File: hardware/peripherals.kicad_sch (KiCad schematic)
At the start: 25 parts, among them J6 Conn_01x02, J7 Conn_01x03, J8 USB_C_Receptacle_USB2.0_14P, SW1 SW_Push, U3 74AHCT1G125, U4 USBLC6-2SC6, U5 DS3231MZ

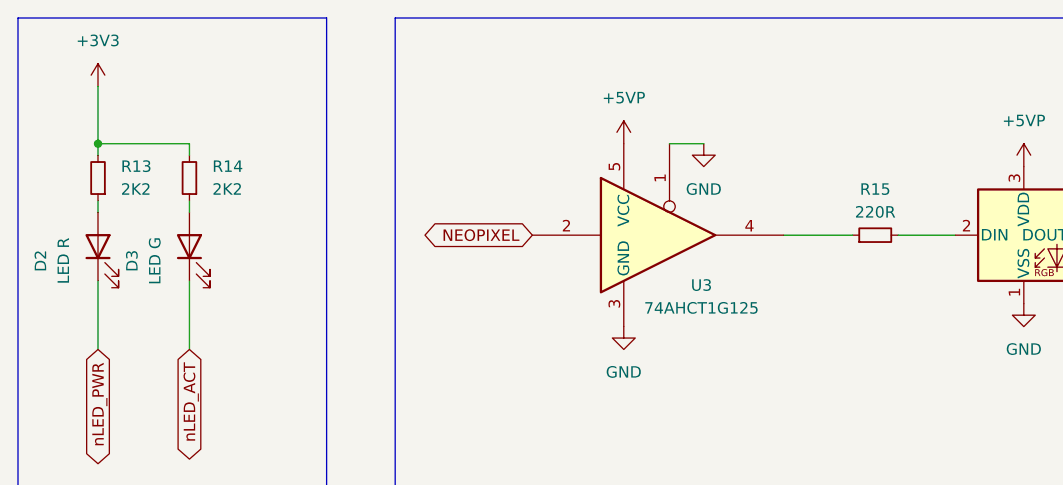
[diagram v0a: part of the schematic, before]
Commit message: Consolidate LED resistors to 330R, eliminate 220R value
R13, R14 (status LEDs): 2K2 → 330R
R15 (NeoPixel data): 220R → 330R
9 unique resistor values (was 10)
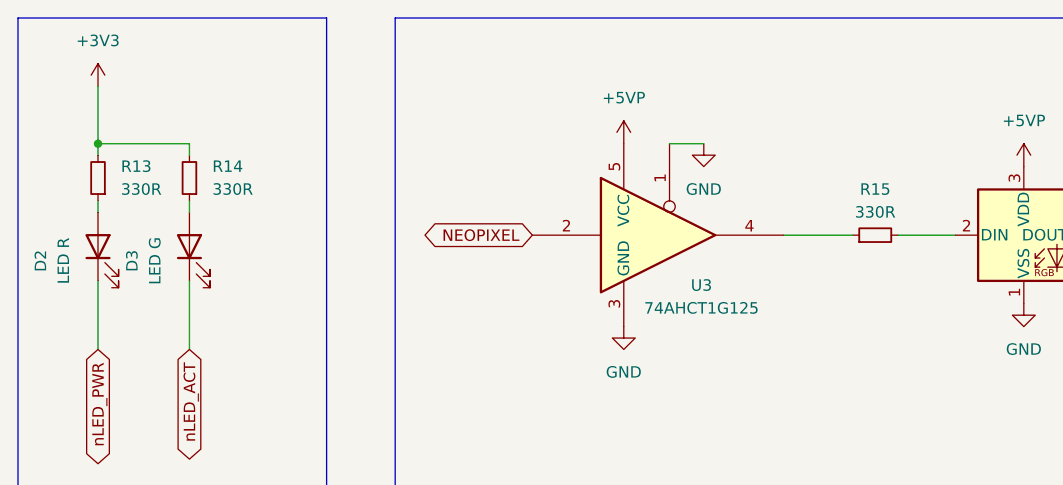
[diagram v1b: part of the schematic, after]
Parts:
- R13, R14: value 2K2 -> 330R
- R15: value 220R -> 330R
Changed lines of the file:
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@@
 			)
 		)
-		(property "Value" "2K2"
+		(property "Value" "330R"
 			(at 36.83 34.2899 0)
 			(show_name no)
@@
 			)
 		)
-		(property "Value" "2K2"
+		(property "Value" "330R"
 			(at 26.67 34.2899 0)
 			(show_name no)
@@
 			)
 		)
-		(property "Value" "220R"
+		(property "Value" "330R"
 			(at 110.49 36.83 90)
 			(show_name no)

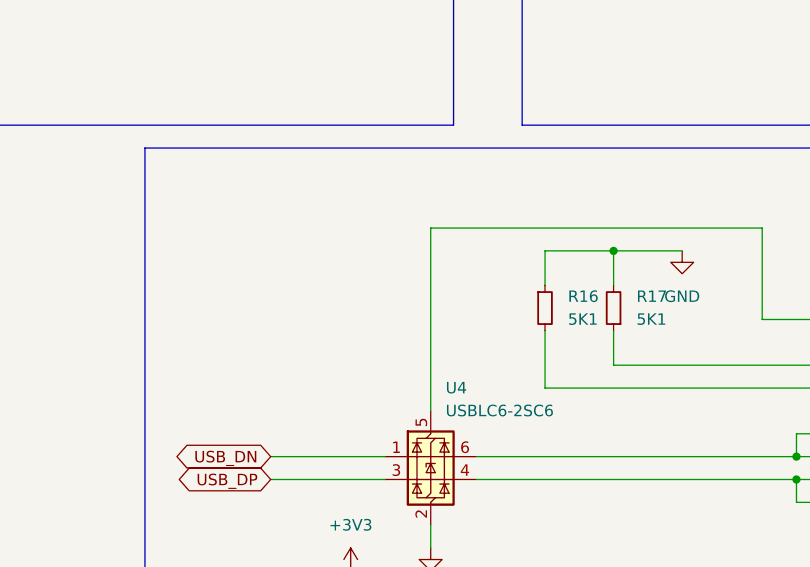
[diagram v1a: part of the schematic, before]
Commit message: Add 100nF decoupling cap on USB VBUS for USBLC6-2SC6
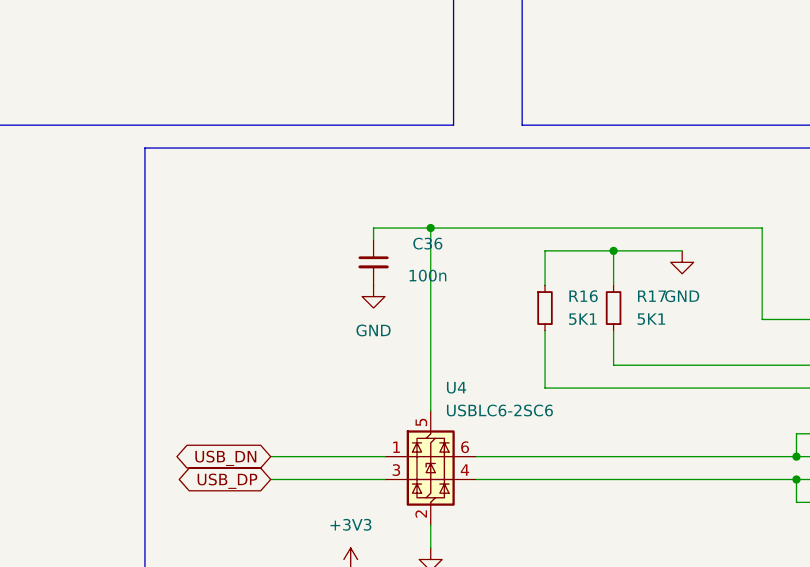
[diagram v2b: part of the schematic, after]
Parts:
- added C36: 100n, Capacitor_SMD:C_0805_2012Metric, symbol Device:C_Small
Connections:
- net GND: now also C36.2
- net at J8.A4 (VBUS), J8.A9 (VBUS), J8.B4 (VBUS)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: now also C36.1
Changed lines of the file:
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@@
 	)
 	(junction
+		(at 161.29 81.28)
+		(diameter 0)
+		(color 0 0 0 0)
+	)
+	(junction
 		(at 24.13 29.21)
 		(diameter 0)
@@
 	(wire
 		(pts
+			(xy 154.94 82.55) (xy 154.94 81.28)
+		)
+		(stroke
+			(width 0)
+			(type default)
+		)
+	)
+	(wire
+		(pts
 			(xy 173.99 83.82) (xy 181.61 83.82)
 		)
@@
 	(wire
 		(pts
+			(xy 154.94 81.28) (xy 161.29 81.28)
+		)
+		(stroke
+			(width 0)
+			(type default)
+		)
+	)
+	(wire
+		(pts
 			(xy 166.37 109.22) (xy 201.93 109.22)
 		)
@@
 	(symbol
 		(lib_id "power:GND")
+		(at 154.94 87.63 0)
+		(unit 1)
+		(body_style 1)
+		(exclude_from_sim no)
+		(in_bom yes)
+		(on_board yes)
+		(in_pos_files yes)
+		(dnp no)
+		(fields_autoplaced yes)
+		(property "Reference" "#PWR073"
+			(at 154.94 93.98 0)
+			(hide yes)
+			(show_name no)
+			(do_not_autoplace no)
+			(effects
+				(font
+					(size 1.27 1.27)
+				)
+			)
+		)
+		(property "Value" "GND"
+			(at 154.94 92.71 0)
+			(show_name no)
+			(do_not_autoplace no)
+			(effects
+				(font
+					(size 1.27 1.27)
+				)
+			)
+		)
+		(property "Footprint" ""
+			(at 154.94 87.63 0)
+			(hide yes)
+			(show_name no)
+			(do_not_autoplace no)
+			(effects
+				(font
+					(size 1.27 1.27)
+				)
+			)
+		)
+		(property "Datasheet" ""
+			(at 154.94 87.63 0)
+			(hide yes)
+			(show_name no)
+			(do_not_autoplace no)
+			(effects
+				(font
+					(size 1.27 1.27)
+				)
+			)
+		)
+		(property "Description" "Power symbol creates a global label with name \"GND\" , ground"
+			(at 154.94 87.63 0)
+			(hide yes)
+			(show_name no)
+			(do_not_autoplace no)
+			(effects
+				(font
+					(size 1.27 1.27)
+				)
+			)
+		)
+		(pin "1"
+		)
+		(instances
+			(project "granit"
+				(path "/d2c135e3-a983-4cd4-8cff-b50ca3c7671a/d4e5f6a7-b8c9-4d0e-1f2a-3b4c5d6e7f80"
+					(reference "#PWR073")
+					(unit 1)
+				)
+			)
+		)
+	)
+	(symbol
+		(lib_id "power:GND")
 		(at 91.44 29.21 0)
 		(unit 1)
@@
 					(unit 1)
 				)
+			)
+		)
+	)
+	(symbol
+		(lib_id "Device:C_Small")
+		(at 154.94 85.09 0)
+		(unit 1)
+		(body_style 1)
+		(exclude_from_sim no)
+		(in_bom yes)
+		(on_board yes)
+		(in_pos_files yes)
+		(dnp no)
+		(property "Reference" "C36"
+			(at 159.258 83.058 0)
+			(show_name no)
+			(do_not_autoplace no)
+			(effects
+				(font
+					(size 1.27 1.27)
+				)
+				(justify left)
+			)
+		)
+		(property "Value" "100n"
+			(at 158.75 86.614 0)
+			(show_name no)
+			(do_not_autoplace no)
+			(effects
+				(font
+					(size 1.27 1.27)
+				)
+				(justify left)
+			)
+		)
+		(property "Footprint" "Capacitor_SMD:C_0805_2012Metric"
+			(at 155.9052 88.9 0)
+			(hide yes)
+			(show_name no)
+			(do_not_autoplace no)
+			(effects
+				(font
+					(size 1.27 1.27)
+				)
+			)
+		)
+		(property "Datasheet" "https://www.samsungsem.com/resources/file/global/support/product_catalog/MLCC.pdf"
+			(at 154.94 85.09 0)
+			(hide yes)
+			(show_name no)
+			(do_not_autoplace no)
+			(effects
+				(font
+					(size 1.27 1.27)
+				)
+			)
+		)
+		(property "Description" "RGB addressable LED (NeoPixel compatible)"
+			(at 154.94 85.09 0)
+			(hide yes)
+			(show_name no)
+			(do_not_autoplace no)
+			(effects
+				(font
+					(size 1.27 1.27)
+				)
+			)
+		)
+		(property "Supplier" "https://www.digikey.ch/de/products/detail/samsung-electro-mechanics/CL21B104KBCNNNC/3886661"
+			(at 154.94 85.09 0)
+			(hide yes)
+			(show_name no)
+			(do_not_autoplace no)
+			(effects
+				(font
+					(size 1.27 1.27)
+				)
+			)
+		)
+		(property "Notes" "10% 16V Ceramic Capacitor X7R"
+			(at 154.94 85.09 0)
+			(hide yes)
+			(show_name no)
+			(do_not_autoplace no)
+			(effects
+				(font
+					(size 1.27 1.27)
+				)
+			)
+		)
+		(property "Digikey" "1276-1180-1-ND"
+			(at 154.94 85.09 0)
+			(hide yes)
+			(show_name no)
+			(do_not_autoplace no)
+			(effects
+				(font
+					(size 1.27 1.27)
+				)
+			)
+		)
+		(pin "1"
+		)
+		(pin "2"
+		)
+		(instances
+			(project "granit"
+				(path "/d2c135e3-a983-4cd4-8cff-b50ca3c7671a/d4e5f6a7-b8c9-4d0e-1f2a-3b4c5d6e7f80"
+					(reference "C36")
+					(unit 1)
+				)

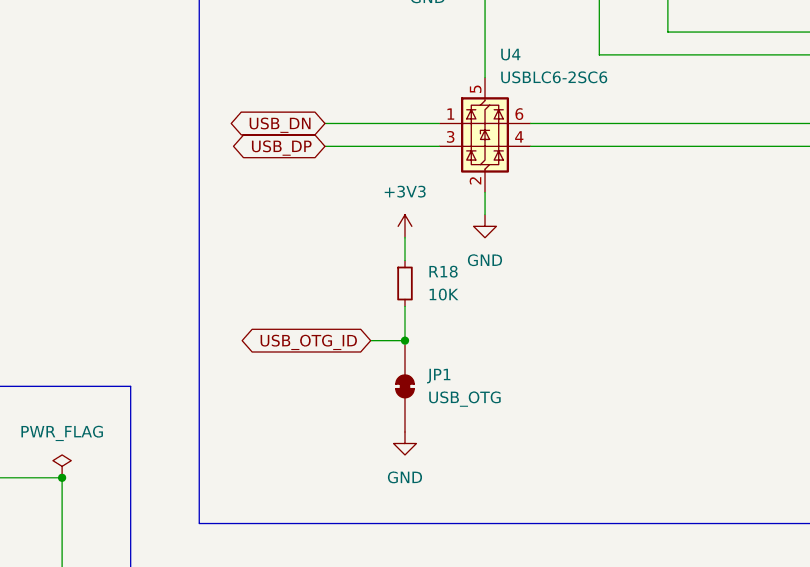
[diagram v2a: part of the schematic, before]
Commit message: Set USB OTG_ID pull-up resistor to DNP (only needed in host mode)
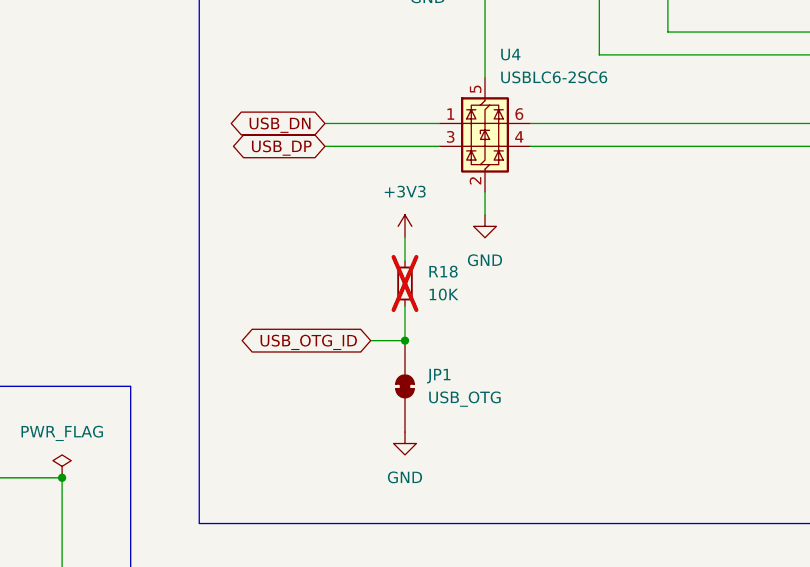
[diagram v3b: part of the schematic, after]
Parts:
- R18: now not fitted
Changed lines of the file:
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@@
 		(on_board yes)
 		(in_pos_files yes)
-		(dnp no)
+		(dnp yes)
 		(fields_autoplaced yes)
 		(property "Reference" "R18"

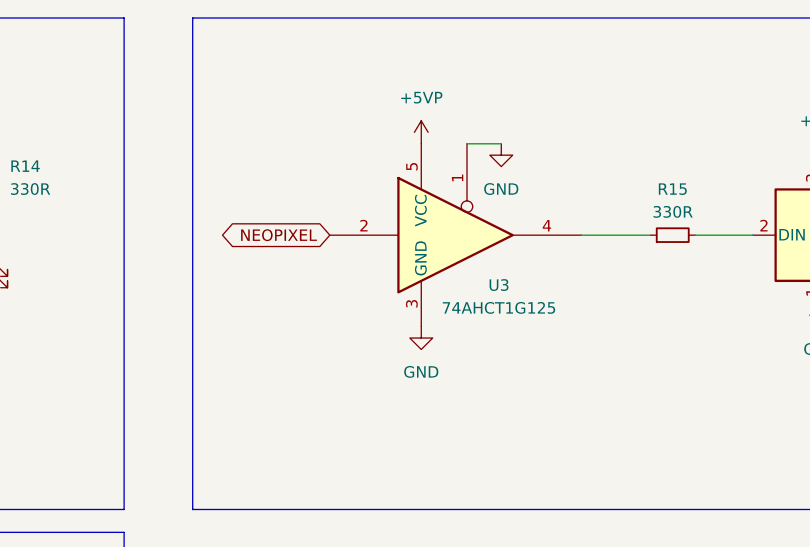
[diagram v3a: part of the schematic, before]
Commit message: Replace 74AHCT1G125 with 74AHCT1G32 for NeoPixel level shifter
OR gate with input B tied to GND acts as buffer.
Same AHCT family, same SOT-23-5 package.
Enables reuse of same part for wake circuit.
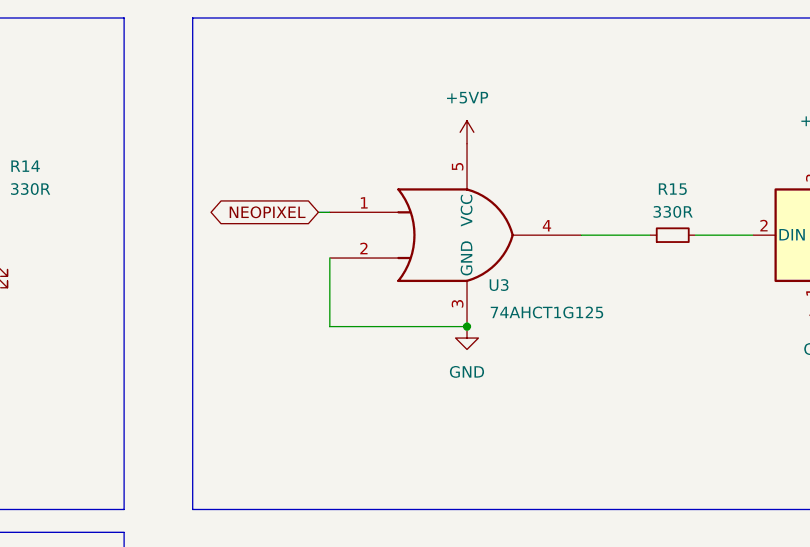
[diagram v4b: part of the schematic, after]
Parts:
- U3: symbol 74xGxx:74AHCT1G125 -> 74xGxx:74AHCT1G32
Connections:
- net GND: now also U3.2; no longer U3.1
- net NEOPIXEL: now also U3.1; no longer U3.2
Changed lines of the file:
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@@
 	)
 	(junction
+		(at 87.63 49.53)
+		(diameter 0)
+		(color 0 0 0 0)
+	)
+	(junction
 		(at 201.93 109.22)
 		(diameter 0)
@@
 	(wire
 		(pts
+			(xy 72.39 41.91) (xy 72.39 49.53)
+		)
+		(stroke
+			(width 0)
+			(type default)
+		)
+	)
+	(wire
+		(pts
 			(xy 24.13 35.56) (xy 24.13 36.83)
 		)
@@
 	(wire
 		(pts
+			(xy 72.39 49.53) (xy 87.63 49.53)
+		)
+		(stroke
+			(width 0)
+			(type default)
+		)
+	)
+	(wire
+		(pts
 			(xy 205.74 96.52) (xy 181.61 96.52)
 		)
@@
 	(wire
 		(pts
-			(xy 87.63 29.21) (xy 91.44 29.21)
+			(xy 71.12 36.83) (xy 72.39 36.83)
 		)
 		(stroke
@@
 	(global_label "NEOPIXEL"
 		(shape bidirectional)
-		(at 72.39 39.37 180)
+		(at 71.12 36.83 180)
 		(fields_autoplaced yes)
 		(effects
@@
 		)
 		(property "Intersheetrefs" "${INTERSHEET_REFS}"
-			(at 59.2221 39.37 0)
+			(at 57.9521 36.83 0)
 			(hide yes)
 			(show_name no)
@@
 	)
 	(symbol
-		(lib_id "74xGxx:74AHCT1G125")
+		(lib_id "74xGxx:74AHCT1G32")
 		(at 87.63 39.37 0)
 		(unit 1)
@@
 		)
 		(property "Value" "74AHCT1G125"
-			(at 91.186 47.498 0)
+			(at 96.52 48.006 0)
 			(show_name no)
 			(do_not_autoplace no)
@@
 			)
 		)
-		(property "Description" "Single Buffer Gate Tri-State, Low-Voltage CMOS"
+		(property "Description" "Single OR Gate, Low-Voltage CMOS"
 			(at 87.63 39.37 0)
 			(hide yes)
@@
 	)
 	(symbol
-		(lib_id "power:GND")
-		(at 91.44 29.21 0)
-		(unit 1)
-		(body_style 1)
-		(exclude_from_sim no)
-		(in_bom yes)
-		(on_board yes)
-		(in_pos_files yes)
-		(dnp no)
-		(fields_autoplaced yes)
-		(property "Reference" "#PWR053"
-			(at 91.44 35.56 0)
-			(hide yes)
-			(show_name no)
-			(do_not_autoplace no)
-			(effects
-				(font
-					(size 1.27 1.27)
-				)
-			)
-		)
-		(property "Value" "GND"
-			(at 91.44 34.29 0)
-			(show_name no)
-			(do_not_autoplace no)
-			(effects
-				(font
-					(size 1.27 1.27)
-				)
-			)
-		)
-		(property "Footprint" ""
-			(at 91.44 29.21 0)
-			(hide yes)
-			(show_name no)
-			(do_not_autoplace no)
-			(effects
-				(font
-					(size 1.27 1.27)
-				)
-			)
-		)
-		(property "Datasheet" ""
-			(at 91.44 29.21 0)
-			(hide yes)
-			(show_name no)
-			(do_not_autoplace no)
-			(effects
-				(font
-					(size 1.27 1.27)
-				)
-			)
-		)
-		(property "Description" "Power symbol creates a global label with name \"GND\" , ground"
-			(at 91.44 29.21 0)
-			(hide yes)
-			(show_name no)
-			(do_not_autoplace no)
-			(effects
-				(font
-					(size 1.27 1.27)
-				)
-			)
-		)
-		(pin "1"
-		)
-		(instances
-			(project "granit"
-				(path "/d2c135e3-a983-4cd4-8cff-b50ca3c7671a/d4e5f6a7-b8c9-4d0e-1f2a-3b4c5d6e7f80"
-					(reference "#PWR053")
-					(unit 1)
-				)
-			)
-		)
-	)
-	(symbol
 		(lib_id "power:+3V3")
 		(at 24.13 22.86 0)
@@
 	(symbol
 		(lib_id "power:GND")
-		(at 82.55 49.53 0)
+		(at 87.63 49.53 0)
 		(unit 1)
 		(body_style 1)
@@
 		(fields_autoplaced yes)
 		(property "Reference" "#PWR058"
-			(at 82.55 55.88 0)
+			(at 87.63 55.88 0)
 			(hide yes)
 			(show_name no)
@@
 		)
 		(property "Value" "GND"
-			(at 82.55 54.61 0)
+			(at 87.63 54.61 0)
 			(show_name no)
 			(do_not_autoplace no)
@@
 		)
 		(property "Footprint" ""
-			(at 82.55 49.53 0)
+			(at 87.63 49.53 0)
 			(hide yes)
 			(show_name no)
@@
 		)
 		(property "Datasheet" ""
-			(at 82.55 49.53 0)
+			(at 87.63 49.53 0)
 			(hide yes)
 			(show_name no)
@@
 		)
 		(property "Description" "Power symbol creates a global label with name \"GND\" , ground"
-			(at 82.55 49.53 0)
+			(at 87.63 49.53 0)
 			(hide yes)
 			(show_name no)
@@
 	(symbol
 		(lib_id "power:+5VP")
-		(at 82.55 29.21 0)
+		(at 87.63 29.21 0)
 		(unit 1)
 		(body_style 1)
@@
 		(fields_autoplaced yes)
 		(property "Reference" "#PWR052"
-			(at 82.55 33.02 0)
+			(at 87.63 33.02 0)
 			(hide yes)
 			(show_name no)
@@
 		)
 		(property "Value" "+5VP"
-			(at 82.55 24.13 0)
+			(at 87.63 24.13 0)
 			(show_name no)
 			(do_not_autoplace no)
@@
 		)
 		(property "Footprint" ""
-			(at 82.55 29.21 0)
+			(at 87.63 29.21 0)
 			(hide yes)
 			(show_name no)
@@
 		)
 		(property "Datasheet" ""
-			(at 82.55 29.21 0)
+			(at 87.63 29.21 0)
 			(hide yes)
 			(show_name no)
@@
 		)
 		(property "Description" "Power symbol creates a global label with name \"+5VP\""
-			(at 82.55 29.21 0)
+			(at 87.63 29.21 0)
 			(hide yes)
 			(show_name no)
